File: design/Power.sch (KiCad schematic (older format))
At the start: 50 parts, among them U2 NCP1117ST33T3G, U3 DRV8302

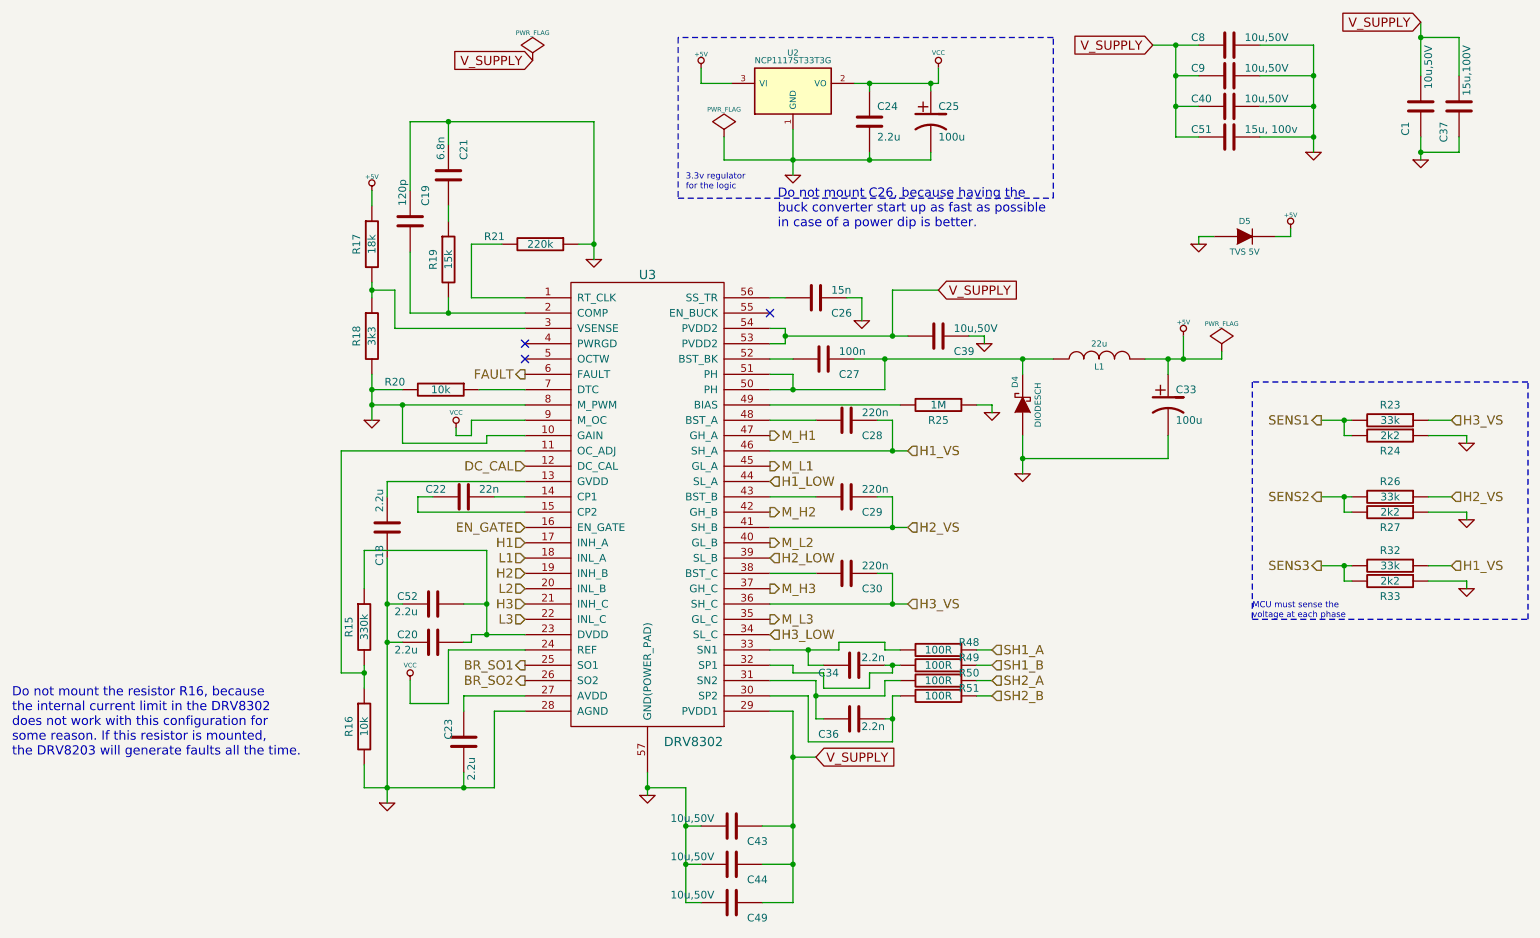
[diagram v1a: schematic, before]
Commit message: Make change in annotations and some small fixes
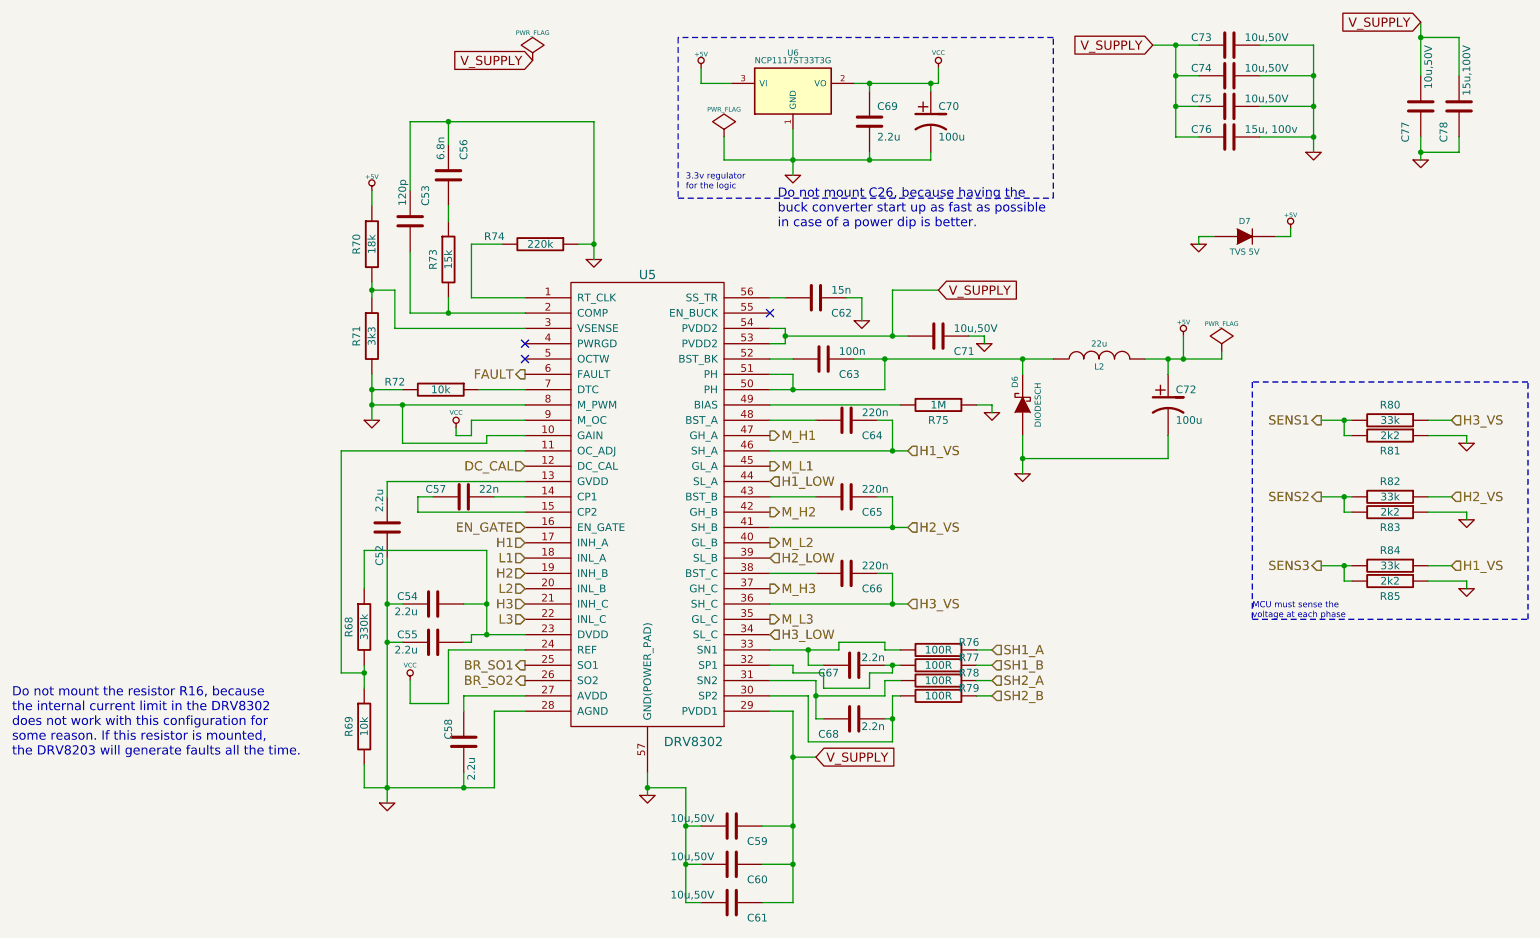
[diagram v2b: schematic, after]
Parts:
- renumbered C19 to C10, C52 to C11, C20 to C12, C21 to C13, C22 to C14, C23 to C15, C43 to C16, C44 to C17, C49 to C18, C26 to C19, C27 to C20, C28 to C21, C29 to C22, C30 to C23, C34 to C24, C36 to C25, C24 to C26, C25 to C27, C39 to C28, C33 to C29, C8 to C30, C9 to C31, C40 to C32, C51 to C33, C1 to C34, C37 to C35, C18 to C9, R15 to R34, R16 to R35, R17 to R36, R18 to R37, R20 to R38, R19 to R39, R21 to R40, R25 to R41, R48 to R42, R49 to R43, R50 to R44, R51 to R45, R23 to R46, R24 to R47, R26 to R48, R27 to R49, R32 to R50, R33 to R51, U3 to U2, U2 to U3
